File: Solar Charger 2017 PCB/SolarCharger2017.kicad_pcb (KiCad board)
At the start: 2 copper layers, 21 parts, among them P1 5V OUT, P2 LiIon Cell V, P3 PV IN 1, P4 PV IN 2, SW1 SPST, U1 BQ24210

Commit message: Update of PCB
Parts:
- added P5: LiIon Cell V, REInnovationFootprint:SIL_2_screw_+_JST_2mm, F.Cu at (185.4, 76.9)
- added P6: 5V OUT, REInnovationFootprint:SIL-2_screw_terminal, F.Cu at (106.0, 76.9)
- BT1: value LiIon Cell -> 18650 LiIon Cell
- DCDC1, DCDC2: value DC-DC_GENERIC -> DC-DC
- P3, P4: footprint REInnovationFootprint:SIL-2_screw_terminal -> REInnovationFootprint:SIL_2_screw_+_JST_2mm
- PCB1: footprint REInnovationFootprint:PCB_65x65mm -> REInnovationFootprint:PCB_65x90mm
- SC1: footprint REInnovationFootprint:PV_130mmx65mm -> REInnovationFootprint:PV_130mmx65mm_NoOutline
- SW1: value SPST -> 5V ON
- moved P3 54.5 mm to (106.0, 101.0), turned to 90 degrees
- moved P4 49.5 mm to (185.4, 96.0)
- moved PCB1 37.2 mm to (98.4, 128.9)
- moved SW1 36.3 mm to (144.1, 69.9)
- moved LG1 35.5 mm to (150.2, 98.3)
- moved P2 35.1 mm to (158.8, 70.6)
- moved C1 35.0 mm to (146.7, 80.1)
- moved DCDC1 35.0 mm to (118.7, 99.8)
- moved DCDC2 35.0 mm to (118.1, 104.8)
- moved P1 35.0 mm to (125.1, 70.6)
- moved C2 35.0 mm to (154.3, 80.1)
- moved U1 35.0 mm to (151.1, 89.0)
- moved SC1 35.0 mm to (80.6, 130.9)
- moved R2 33.1 mm to (144.1, 88.3)
- moved R1 33.1 mm to (141.0, 88.3)
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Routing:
- net GND: track 0.00 -> 219.5 mm
- net VCC: track 0.00 -> 163.4 mm
- net Net-(C1-Pad1): track 0.00 -> 123.6 mm
- net Net-(D2-Pad1): track 0.00 -> 60.3 mm, vias 0 -> 1
- net Net-(D3-Pad1): track 0.00 -> 60.1 mm, vias 0 -> 1
- net Net-(DCDC1-Pad1): track 0.00 -> 48.6 mm
- net Net-(D2-Pad2): track 0.00 -> 40.4 mm
- net Net-(DCDC1-Pad3): track 0.00 -> 37.4 mm
- net Net-(DCDC1-Pad4): track 0.00 -> 34.2 mm
- net Net-(D3-Pad2): track 0.00 -> 29.8 mm
- net Net-(R1-Pad1): track 0.00 -> 11.6 mm
- net Net-(R2-Pad2): track 0.00 -> 11.1 mm, vias 0 -> 1
- net Net-(R2-Pad1): track 0.00 -> 7.19 mm
- added copper zone on B.Cu, net GND
- added copper zone on F.Cu, net GND
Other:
- board outline added: 95 x 65 mm
- net class Default: clearance 0.2 -> 0.1; trace_width 0.25 -> 0.762; via_dia 0.6 -> 0.635; via_drill 0.4 -> 0.508
- rule trace_clearance: 0.2 -> 0.1
- board text added: "+"
- board text added: "12/6/2017"
- board text added: "@curiouselectric"
- board text added: "DIY SOLAR CHARGER"
- board text added: "curiouselectric.co.uk"

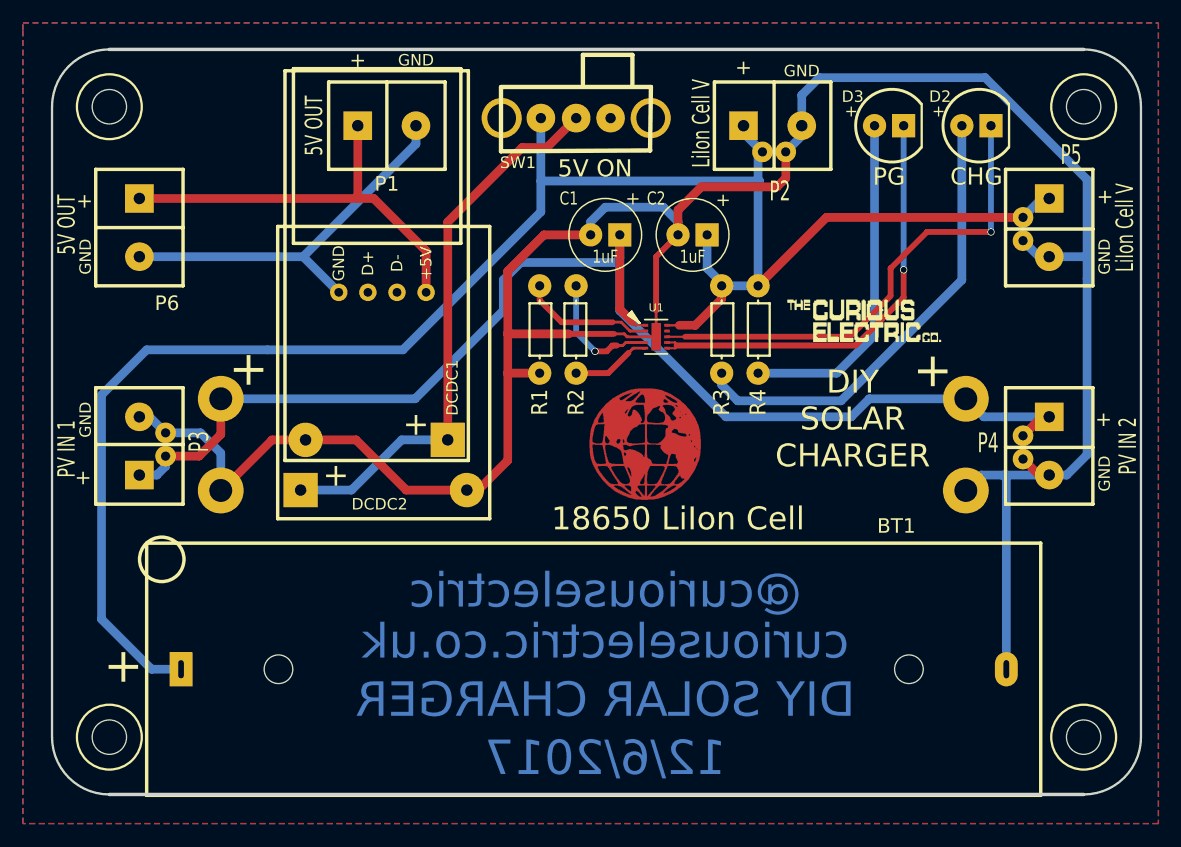
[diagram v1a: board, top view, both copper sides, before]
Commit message: Changes to PCB
DC-DC converter correct. Moved silkscreen. Sorted costs
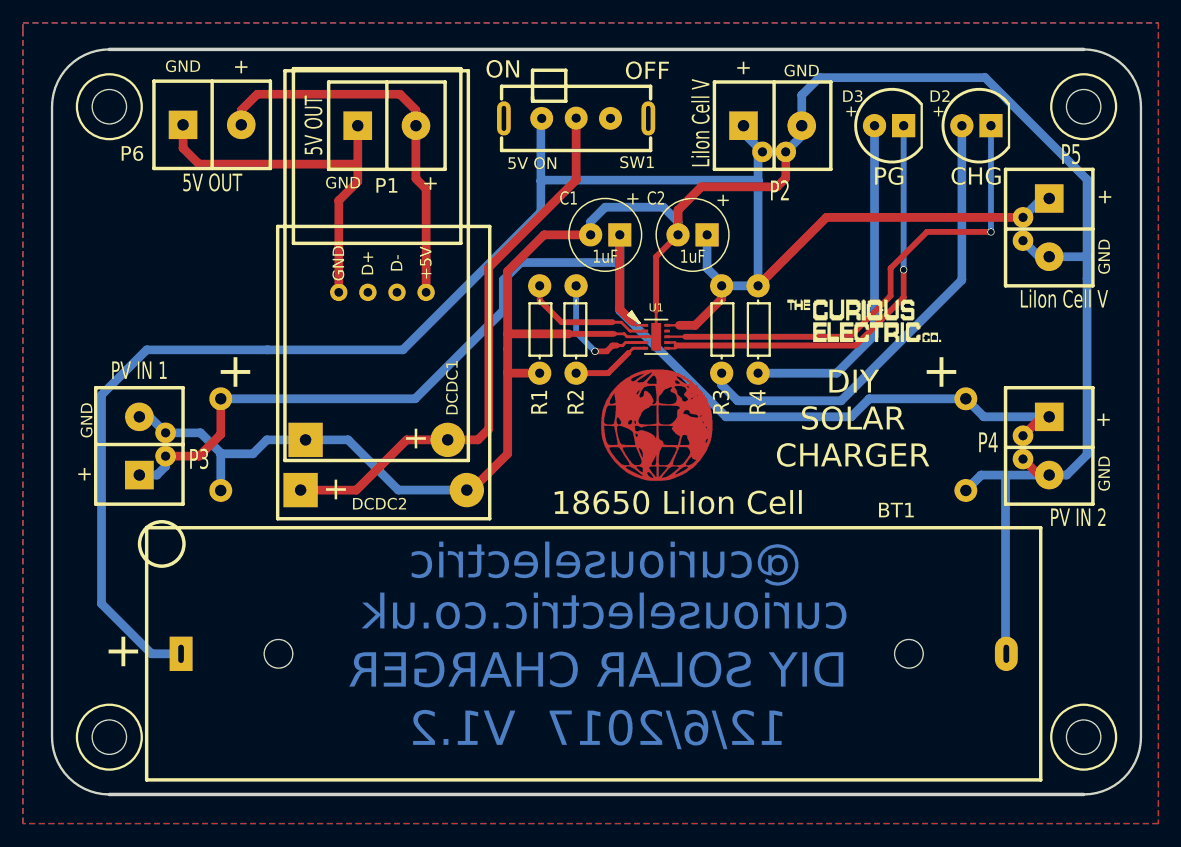
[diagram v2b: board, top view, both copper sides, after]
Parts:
- DCDC1: footprint REInnovationFootprint:TH_DCDC_Converter_USB -> TH_DCDC_Converter_USB
- DCDC2: footprint REInnovationFootprint:TH_DCDC_Converter_NoUSB -> TH_DCDC_Converter_NoUSB
- SC1: footprint REInnovationFootprint:PV_130mmx65mm_NoOutline -> PV_130mmx65mm_NoOutline
- SW1: footprint matts_components:SW_SPDT_rapid_760271 -> REInnovationFootprint:SW_SPDT_R_Angle_ALIEX
- moved P6 7.47 mm to (109.9, 70.5), turned to 0 degrees
- moved LG1 1.94 mm to (151.3, 96.6)
- moved BT1 1.34 mm to (106.7, 127.6)
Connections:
- DCDC1 pad 1: Net-(DCDC1-Pad1) -> GND
- DCDC1 pad 2: GND -> Net-(DCDC1-Pad2)
- DCDC2 pad 1: Net-(DCDC1-Pad1) -> GND
- DCDC2 pad 2: GND -> Net-(DCDC1-Pad2)
- P1 pad 1: Net-(DCDC1-Pad3) -> Net-(DCDC1-Pad4)
- P1 pad 2: Net-(DCDC1-Pad4) -> Net-(DCDC1-Pad3)
- P6 pad 1: Net-(DCDC1-Pad3) -> Net-(DCDC1-Pad4)
- P6 pad 2: Net-(DCDC1-Pad4) -> Net-(DCDC1-Pad3)
- SW1 pad 2: Net-(DCDC1-Pad1) -> Net-(DCDC1-Pad2)
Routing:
- net Net-(DCDC1-Pad2): track 0.00 -> 49.0 mm
- net Net-(DCDC1-Pad1): track 48.6 -> 0.00 mm
- net Net-(DCDC1-Pad3): track 37.4 -> 33.9 mm
- net GND: track 219.5 -> 217.2 mm
- net VCC: track 163.4 -> 162.0 mm
- net Net-(DCDC1-Pad4): track 34.2 -> 33.1 mm
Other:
- board text added: "12/6/2017 V1.2"
- board text added: "OFF"
- board text added: "ON"
- board text removed: "12/6/2017"

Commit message: Update of Gerber
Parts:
- moved P6 12.7 mm to (106.0, 82.5), turned to 90 degrees
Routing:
- net Net-(DCDC1-Pad3): track 33.9 -> 43.7 mm
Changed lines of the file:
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@@
     (links 47)
     (no_connects 0)
-    (area 80.295 53.195261 206.8844 131.445001)
+    (area 80.295 61.595 194.945001 131.445001)
     (thickness 1.6)
     (drawings 9)
-    (tracks 206)
+    (tracks 205)
     (zones 0)
     (modules 23)
@@
   )
   (module REInnovationFootprint:SIL-2_screw_terminal (layer F.Cu)
-    (at 109.855 70.485)
+    (at 106.045 82.55 90)
     (descr "Connecteurs 2 pins")
     (tags "CONN DEV")
-    (fp_text reference P6 (at -4.445 2.54 180) (layer F.SilkS)
+    (fp_text reference P6 (at -1.27 5.715 270) (layer F.SilkS)
       (effects (font (thickness 0.3048)))
     )
-    (fp_text value "5V OUT" (at 2.54 5.08) (layer F.SilkS)
+    (fp_text value "5V OUT" (at 8.89 0 180) (layer F.SilkS)
       (effects (font (size 1.524 1.016) (thickness 0.254)))
     )
@@
     (fp_line (start 2.54 -3.81) (end 2.54 3.81) (layer F.SilkS) (width 0.3))
     (fp_line (start -2.54 3.81) (end -2.54 -3.81) (layer F.SilkS) (width 0.3))
-    (fp_text user GND (at 0 -5.08 180) (layer F.SilkS)
+    (fp_text user GND (at 0 -5.08 270) (layer F.SilkS)
       (effects (font (size 1 1) (thickness 0.25)))
     )
-    (fp_text user + (at 5.08 -5.08) (layer F.SilkS)
+    (fp_text user + (at 5.08 -5.08 90) (layer F.SilkS)
       (effects (font (thickness 0.3048)))
     )
-    (pad 1 thru_hole rect (at 0 0) (size 2.49936 2.49936) (drill 1.00076) (layers *.Cu *.Mask F.SilkS)
+    (pad 1 thru_hole rect (at 0 0 90) (size 2.49936 2.49936) (drill 1.00076) (layers *.Cu *.Mask F.SilkS)
       (net 12 "Net-(DCDC1-Pad4)"))
-    (pad 2 thru_hole circle (at 5.08 0) (size 2.49936 2.49936) (drill 1.00076) (layers *.Cu *.Mask F.SilkS)
+    (pad 2 thru_hole circle (at 5.08 0 90) (size 2.49936 2.49936) (drill 1.00076) (layers *.Cu *.Mask F.SilkS)
       (net 11 "Net-(DCDC1-Pad3)"))
   )
@@
   (segment (start 171.577 85.419) (end 171.577 83.006) (width 0.2) (layer F.Cu) (net 10))
   (segment (start 168.021 88.975) (end 171.577 85.419) (width 0.2) (layer F.Cu) (net 10))
+  (segment (start 106.045 77.47) (end 126.365 77.47) (width 0.762) (layer B.Cu) (net 11))
+  (segment (start 130.175 73.66) (end 130.175 70.56) (width 0.762) (layer B.Cu) (net 11))
+  (segment (start 126.365 77.47) (end 130.175 73.66) (width 0.762) (layer B.Cu) (net 11))
   (segment (start 131.06 85.1) (end 131.06 76.069) (width 0.762) (layer F.Cu) (net 11))
   (segment (start 130.175 75.184) (end 130.175 70.56) (width 0.762) (layer F.Cu) (net 11))
   (segment (start 131.06 76.069) (end 130.175 75.184) (width 0.762) (layer F.Cu) (net 11))
-  (segment (start 114.935 70.485) (end 114.935 69.215) (width 0.762) (layer F.Cu) (net 11))
-  (segment (start 130.175 69.215) (end 130.175 70.56) (width 0.762) (layer F.Cu) (net 11))
-  (segment (start 128.778 67.818) (end 130.175 69.215) (width 0.762) (layer F.Cu) (net 11))
-  (segment (start 116.332 67.818) (end 128.778 67.818) (width 0.762) (layer F.Cu) (net 11))
-  (segment (start 114.935 69.215) (end 116.332 67.818) (width 0.762) (layer F.Cu) (net 11))
-  (segment (start 109.855 70.485) (end 109.855 72.517) (width 0.762) (layer F.Cu) (net 12))
-  (segment (start 111.252 73.914) (end 125.095 73.914) (width 0.762) (layer F.Cu) (net 12))
-  (segment (start 109.855 72.517) (end 111.252 73.914) (width 0.762) (layer F.Cu) (net 12))
-  (segment (start 123.44 85.1) (end 123.44 77.093) (width 0.762) (layer F.Cu) (net 12))
+  (segment (start 106.045 82.55) (end 123.44 82.55) (width 0.762) (layer F.Cu) (net 12))
+  (segment (start 123.44 82.55) (end 123.19 82.55) (width 0.762) (layer F.Cu) (net 12))
+  (segment (start 123.19 82.55) (end 123.44 82.55) (width 0.762) (layer F.Cu) (net 12))
+  (segment (start 123.44 85.1) (end 123.44 82.55) (width 0.762) (layer F.Cu) (net 12))
+  (segment (start 123.44 82.55) (end 123.44 77.093) (width 0.762) (layer F.Cu) (net 12))
   (segment (start 125.095 75.438) (end 125.095 73.914) (width 0.762) (layer F.Cu) (net 12))
   (segment (start 125.095 73.914) (end 125.095 70.56) (width 0.762) (layer F.Cu) (net 12))

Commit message: Updated PCB
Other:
- board text added: "PV 1"
- board text added: "PV 2"
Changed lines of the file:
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@@
     (area 80.295 61.595 194.945001 131.445001)
     (thickness 1.6)
-    (drawings 9)
+    (drawings 11)
     (tracks 205)
     (zones 0)
@@
     (descr "Connecteurs 2 pins")
     (tags "CONN DEV")
-    (fp_text reference P3 (at 1.345 5.207 180) (layer F.SilkS)
+    (fp_text reference P3 (at -4.243 -1.778 180) (layer F.SilkS)
       (effects (font (size 1.72974 1.08712) (thickness 0.27178)))
     )
-    (fp_text value "PV IN 1" (at 9.092 0 180) (layer F.SilkS)
+    (fp_text value "PV IN 1" (at 8.965 -0.762 180) (layer F.SilkS)
       (effects (font (size 1.524 1.016) (thickness 0.254)))
     )
@@
     (descr "Connecteurs 2 pins")
     (tags "CONN DEV")
-    (fp_text reference P4 (at 2.286 5.334 540) (layer F.SilkS)
+    (fp_text reference P4 (at 9.196 -2.667 540) (layer F.SilkS)
       (effects (font (size 1.72974 1.08712) (thickness 0.27178)))
     )
-    (fp_text value "PV IN 2" (at 8.815 -2.54 540) (layer F.SilkS)
+    (fp_text value "PV IN 2" (at -3.758 -0.889 540) (layer F.SilkS)
       (effects (font (size 1.524 1.016) (thickness 0.254)))
     )
@@
     (pad 5 thru_hole oval (at 0 6.3 90) (size 3 1.2) (drill oval 2.2 0.4) (layers *.Cu *.Mask F.SilkS))
   )
+  (gr_text "PV 2" (at 178.181 98.171 90) (layer F.SilkS)
+    (effects (font (size 1.5 1.5) (thickness 0.3)))
+  )
+  (gr_text "PV 1" (at 113.157 98.298 90) (layer F.SilkS)
+    (effects (font (size 1.5 1.5) (thickness 0.3)))
+  )
   (gr_text OFF (at 150.368 65.786) (layer F.SilkS)

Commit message: Update of instructions
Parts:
- added P7: USB_A, Connectors:USB_A, F.Cu at (125.7, 56.5)
- DCDC1: footprint TH_DCDC_Converter_USB -> REInnovationFootprint:TH_DCDC_Converter_USB
- DCDC2: footprint TH_DCDC_Converter_NoUSB -> REInnovationFootprint:TH_DCDC_Converter_NoUSB
- SC1: footprint PV_130mmx65mm_NoOutline -> REInnovationFootprint:PV_130mmx65mm_NoOutline
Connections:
- LG1 pad 1: (no net) -> Net-(LG1-Pad1)
- U1 pad 9: (no net) -> Net-(U1-Pad9)
